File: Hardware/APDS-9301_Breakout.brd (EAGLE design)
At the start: 12.7 x 15.2 mm, 14 parts, among them U1 APDS-9301

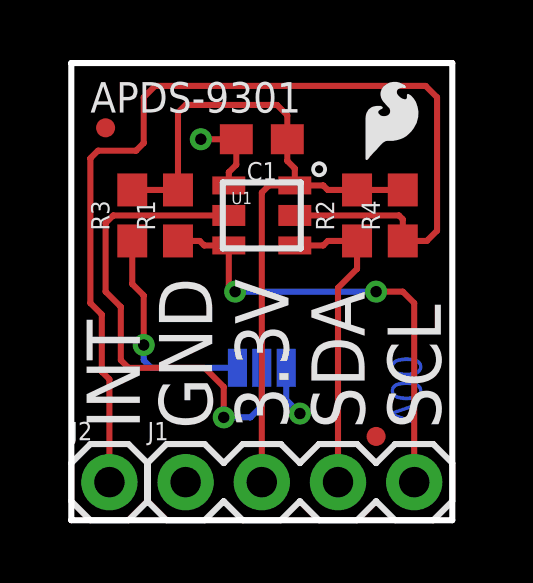
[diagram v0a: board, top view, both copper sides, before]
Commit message: Change to V10, chg silk on back of board
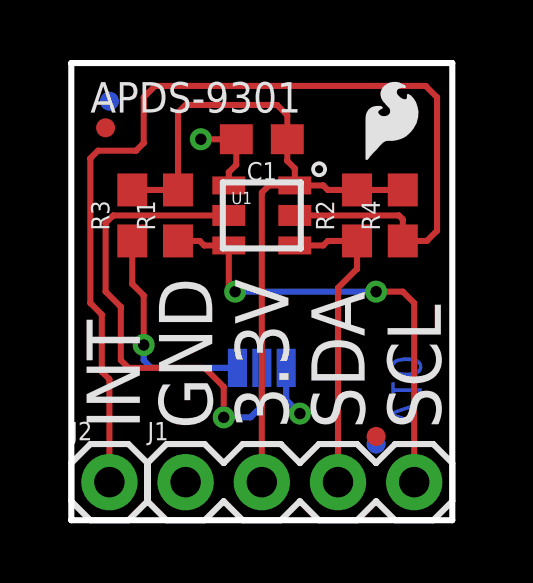
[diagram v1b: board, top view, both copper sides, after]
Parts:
- added FD3, FD4: FIDUCIALUFIDUCIAL, SparkFun-Aesthetics:FIDUCIAL-MICRO
- moved FRAME1 75.5 mm to (-26.7, -16.5)
- moved LOGO2 0.81 mm to (10.7, 13.3)
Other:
- board text added: "ADDR 0x29 - LOW 0x39 - FLOAT 0x49 - HIGH"
- board text added: "v10"
- board text removed: "JP1"
- board text removed: "v00"
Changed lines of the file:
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@@
 <?xml version="1.0" encoding="utf-8"?>
 <!DOCTYPE eagle SYSTEM "eagle.dtd">
-<eagle version="7.7.0">
+<eagle version="7.6.0">
 <drawing>
 <settings>
@@
 <text x="4.064" y="5.08" size="1.016" layer="22" font="vector" ratio="15" rot="MR90" align="center">HIGH</text>
 <text x="8.636" y="5.08" size="1.016" layer="22" font="vector" ratio="15" rot="MR90" align="center">LOW</text>
-<text x="-69.85" y="-25.4" size="1.778" layer="51" font="vector" ratio="15">M. Hord</text>
+<text x="5.08" y="-16.51" size="1.778" layer="51" font="vector" ratio="15">M. Hord</text>
 <dimension x1="0" y1="15.24" x2="12.7" y2="15.24" x3="6.35" y3="19.05" textsize="1.778" textratio="15" layer="47" dtype="horizontal" unit="inch"/>
 <dimension x1="0" y1="15.24" x2="0" y2="0" x3="-3.81" y3="7.62" textsize="1.778" textratio="15" layer="47" dtype="horizontal" unit="inch"/>
-<text x="10.668" y="3.175" size="1.016" layer="16" font="vector" ratio="15" rot="MR90">v00</text>
-<text x="7.366" y="6.223" size="0.8128" layer="22" font="vector" ratio="15" rot="MR0">JP1</text>
+<text x="10.668" y="3.175" size="1.016" layer="16" font="vector" ratio="15" rot="MR90">v10</text>
+<text x="9.652" y="7.62" size="0.8128" layer="22" font="vector" ratio="15" distance="25" rot="MR0">ADDR
+0x29 - LOW
+0x39 - FLOAT
+0x49 - HIGH</text>
 </plain>
 <attributes>
@@
 <attribute name="PROD_ID" value="CAP-08604" x="6.35" y="12.7" size="1.778" layer="27" rot="R180" display="off"/>
 </element>
-<element name="FRAME1" library="SparkFun-Aesthetics" package="CREATIVE_COMMONS" value="FRAME-LETTER" x="-101.6" y="-25.4"/>
+<element name="FRAME1" library="SparkFun-Aesthetics" package="CREATIVE_COMMONS" value="FRAME-LETTER" x="-26.67" y="-16.51"/>
 <element name="JP1" library="SparkFun-Jumpers" package="SMT-JUMPER_3_NO_SILK" value="JUMPER-SMT_3_NO_SILK" x="6.35" y="5.08" rot="MR0"/>
 <element name="R1" library="SparkFun-Resistors" package="0603" value="4.7k" x="3.556" y="10.16" rot="R90">
@@
 <element name="J2" library="SparkFun-Connectors" package="1X01" value="" x="1.27" y="1.27"/>
 <element name="LOGO1" library="SparkFun-Aesthetics" package="SFE_LOGO_FLAME_.1" value="SFE_LOGO_FLAME.1_INCH" x="9.525" y="11.684"/>
-<element name="LOGO2" library="SparkFun-Aesthetics" package="OSHW-LOGO-S" value="OSHW-LOGOS" x="10.16" y="12.7" rot="MR0"/>
+<element name="LOGO2" library="SparkFun-Aesthetics" package="OSHW-LOGO-S" value="OSHW-LOGOS" x="10.668" y="13.335" rot="MR0"/>
 <element name="FD1" library="SparkFun-Aesthetics" package="FIDUCIAL-MICRO" value="FIDUCIALUFIDUCIAL" x="1.143" y="13.081"/>
 <element name="FD2" library="SparkFun-Aesthetics" package="FIDUCIAL-MICRO" value="FIDUCIALUFIDUCIAL" x="10.16" y="2.794"/>
+<element name="FD3" library="SparkFun-Aesthetics" package="FIDUCIAL-MICRO" value="FIDUCIALUFIDUCIAL" x="1.27" y="13.97" rot="MR0"/>
+<element name="FD4" library="SparkFun-Aesthetics" package="FIDUCIAL-MICRO" value="FIDUCIALUFIDUCIAL" x="10.16" y="2.54" rot="MR0"/>
 </elements>
 <signals>
@@
 </board>
 </drawing>
+<compatibility>
+<note version="6.3" minversion="6.2.2" severity="warning">
+Since Version 6.2.2 text objects can contain more than one line,
+which will not be processed correctly with this version.
+</note>
+</compatibility>
 </eagle>

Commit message: Changes for V10 post checklist
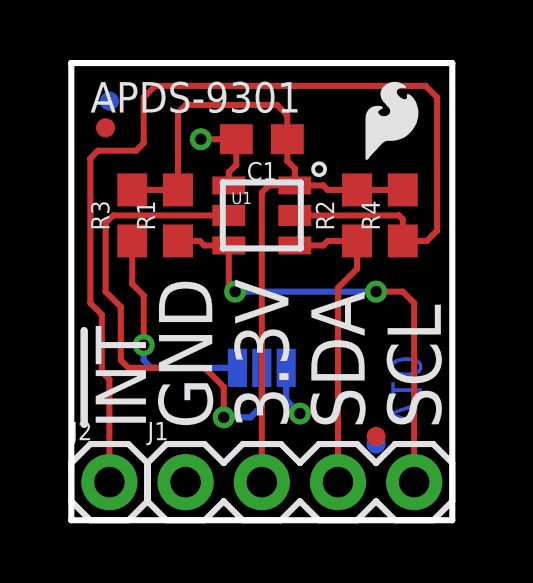
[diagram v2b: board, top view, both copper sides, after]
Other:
- board text added: "!INT"
- board text removed: "INT"
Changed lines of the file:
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@@
 <?xml version="1.0" encoding="utf-8"?>
 <!DOCTYPE eagle SYSTEM "eagle.dtd">
-<eagle version="7.6.0">
+<eagle version="7.7.0">
 <drawing>
 <settings>
@@
 <board>
 <plain>
-<text x="1.397" y="3.048" size="1.778" layer="21" font="vector" ratio="15" rot="R90" align="center-left">INT</text>
+<text x="1.651" y="3.048" size="1.6764" layer="21" font="vector" ratio="15" rot="R90" align="center-left">!INT</text>
 <text x="3.81" y="3.048" size="1.778" layer="21" font="vector" ratio="15" rot="R90" align="center-left">GND</text>
 <text x="6.35" y="3.048" size="1.778" layer="21" font="vector" ratio="15" rot="R90" align="center-left">3.3V</text>
